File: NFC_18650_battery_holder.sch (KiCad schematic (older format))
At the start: 2 parts

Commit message: Schematic done.
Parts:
- added J?: Conn_01x06_Female, symbol Connector:Conn_01x06_Female
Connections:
- net at AE?.1: now also U?.3 (AC1)
- net at AE?.2: now also U?.2 (AC0)
- net Sheet5FAF080E/BATT_RET: now reaches U?.4 (VSS)
- net Sheet5FAF080E/BATT_RET: now also J?.6 (Pin_6)
- net at U?.5 (SDA): now also J?.5 (Pin_5)
- net at U?.6 (SCL): now also J?.4 (Pin_4)
- net at U?.7 (GPO_(OD)): now also J?.3 (Pin_3)
- net at U?.8 (VCC): now also J?.2 (Pin_2)
- new net +BATT: J?.1 (Pin_1)
- no-connect marks 0 -> 1
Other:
- moved on the sheet: AE?, U?
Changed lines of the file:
@@
 $Descr A4 11693 8268
 encoding utf-8
-Sheet 1 1
+Sheet 1 2
 Title ""
 Date ""
@@
 L Device:Antenna_Loop AE?
 U 1 1 5FAE3919
-P 6700 2400
-F 0 "AE?" H 6930 2414 50  0000 L CNN
-F 1 "Antenna_Loop" H 6930 2323 50  0000 L CNN
-F 2 "" H 6700 2400 50  0001 C CNN
-F 3 "~" H 6700 2400 50  0001 C CNN
-	1    6700 2400
+P 7050 2400
+F 0 "AE?" H 7280 2414 50  0000 L CNN
+F 1 "Antenna_Loop" H 7280 2323 50  0000 L CNN
+F 2 "" H 7050 2400 50  0001 C CNN
+F 3 "~" H 7050 2400 50  0001 C CNN
+	1    7050 2400
 	1    0    0    -1
 $EndComp
@@
 L NFC_18659_battery_holder:ST25DV_8p U?
 U 1 1 5FAE5573
-P 8600 2550
-F 0 "U?" H 8600 2565 50  0000 C CNN
-F 1 "ST25DV_8p" H 8600 2474 50  0000 C CNN
-F 2 "" H 8600 2550 50  0001 C CNN
-F 3 "" H 8600 2550 50  0001 C CNN
-	1    8600 2550
+P 8150 2800
+F 0 "U?" H 8150 2815 50  0000 C CNN
+F 1 "ST25DV_8p" H 8150 2724 50  0000 C CNN
+F 2 "" H 8150 2800 50  0001 C CNN
+F 3 "" H 8150 2800 50  0001 C CNN
+	1    8150 2800
 	1    0    0    -1
 $EndComp
+$Sheet
+S 5550 3000 1050 500
+U 5FAF080F
+F0 "Sheet5FAF080E" 50
+F1 "battery_3s_18650.sch" 50
+F2 "BATT_OUT" I R 6600 3100 50
+F3 "BATT_RET" I R 6600 3350 50
+$EndSheet
+Wire Wire Line
+	7650 3150 7150 3150
+Wire Wire Line
+	7150 3150 7150 2600
+Wire Wire Line
+	7050 2600 7050 3250
+Wire Wire Line
+	7050 3250 7650 3250
+Wire Wire Line
+	7650 3350 7350 3350
+$Comp
+L power:+BATT #PWR?
+U 1 1 5FAF9693
+P 6800 2900
+F 0 "#PWR?" H 6800 2750 50  0001 C CNN
+F 1 "+BATT" H 6815 3073 50  0000 C CNN
+F 2 "" H 6800 2900 50  0001 C CNN
+F 3 "" H 6800 2900 50  0001 C CNN
+	1    6800 2900
+	1    0    0    -1
+$EndComp
+Wire Wire Line
+	6800 3100 6800 2900
+Wire Wire Line
+	6600 3100 6800 3100
+Wire Wire Line
+	9400 3350 8650 3350
+Wire Wire Line
+	8650 3250 9400 3250
+Wire Wire Line
+	9400 3150 8650 3150
+Wire Wire Line
+	8650 3050 9400 3050
+Wire Wire Line
+	9400 2950 9100 2950
+Wire Wire Line
+	9100 2950 9100 2800
+$Comp
+L power:+BATT #PWR?
+U 1 1 5FAFB912
+P 9100 2800
+F 0 "#PWR?" H 9100 2650 50  0001 C CNN
+F 1 "+BATT" H 9115 2973 50  0000 C CNN
+F 2 "" H 9100 2800 50  0001 C CNN
+F 3 "" H 9100 2800 50  0001 C CNN
+	1    9100 2800
+	1    0    0    -1
+$EndComp
+$Comp
+L Connector:Conn_01x06_Female J?
+U 1 1 5FAFC15A
+P 9600 3150
+F 0 "J?" H 9628 3126 50  0000 L CNN
+F 1 "Conn_01x06_Female" H 9628 3035 50  0000 L CNN
+F 2 "" H 9600 3150 50  0001 C CNN
+F 3 "~" H 9600 3150 50  0001 C CNN
+	1    9600 3150
+	1    0    0    -1
+$EndComp
+Wire Wire Line
+	9400 3450 9250 3450
+Wire Wire Line
+	9250 3450 9250 3650
+Wire Wire Line
+	9250 3650 7350 3650
+Wire Wire Line
+	7350 3650 7350 3350
+Connection ~ 7350 3350
+Wire Wire Line
+	7350 3350 6600 3350
+NoConn ~ 7650 3050
 $EndSCHEMATC

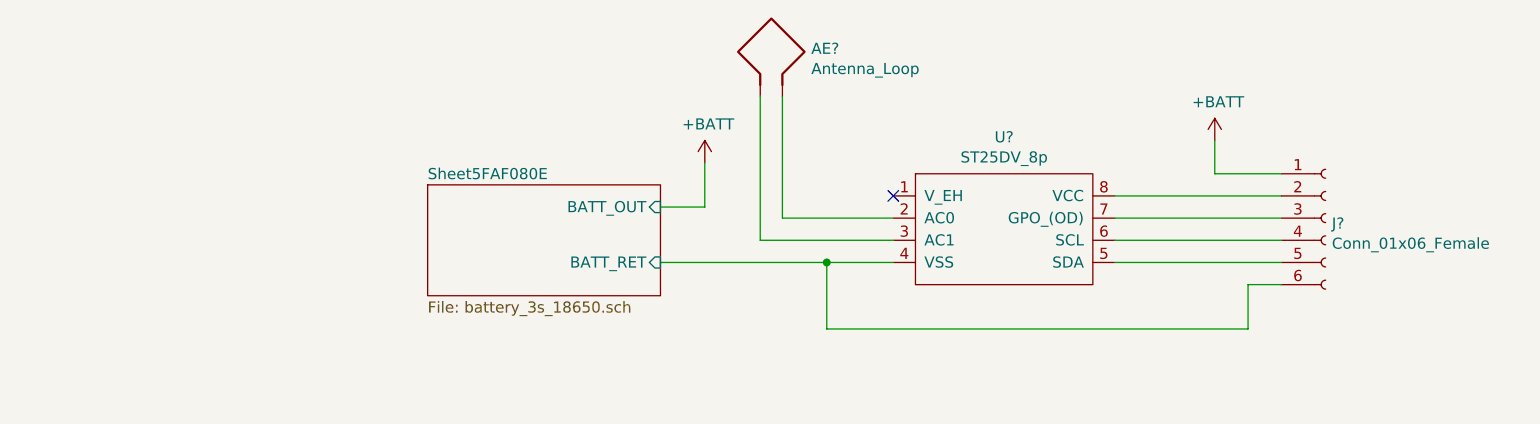
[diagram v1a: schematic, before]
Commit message: Library files added from NFC_hatch projekt. Started to work at the layout. 18650 holder footprint became wider 18 to 22mm.
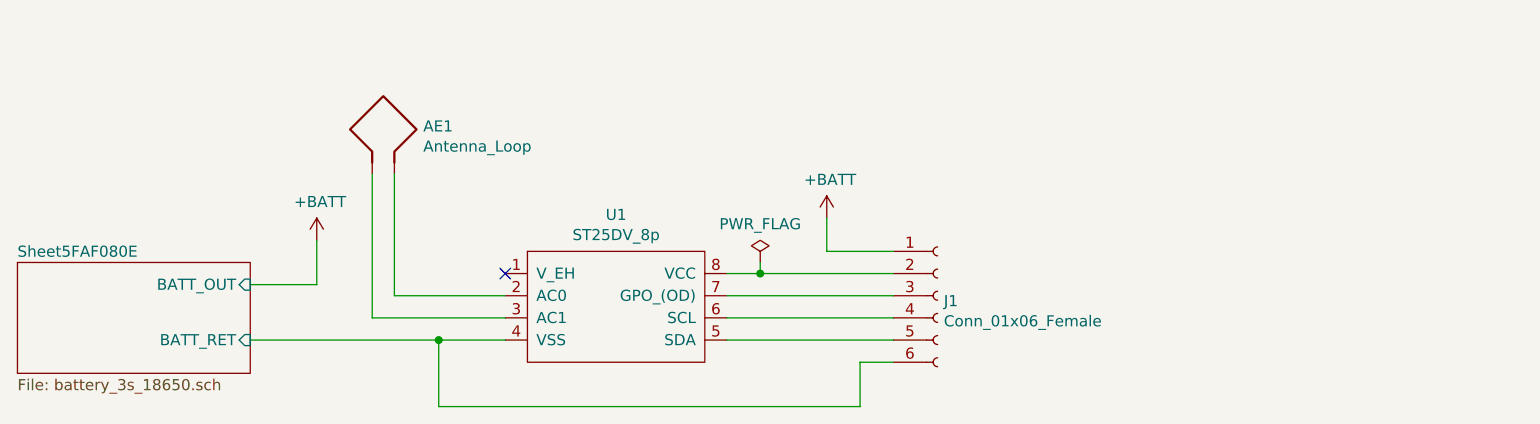
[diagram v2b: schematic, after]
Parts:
- J1: renamed from J?; footprint (none) -> Connector_JST:JST_XH_B6B-XH-A_1x06_P2.50mm_Vertical
- U1: renamed from U?; footprint (none) -> Package_SO:TSSOP-8_4.4x3mm_P0.65mm
- gave numbers to parts that had none: 1
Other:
- moved on the sheet: AE1, J1, U1
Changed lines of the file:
@@
 $EndDescr
 $Comp
-L Device:Antenna_Loop AE?
+L Device:Antenna_Loop AE1
 U 1 1 5FAE3919
-P 7050 2400
-F 0 "AE?" H 7280 2414 50  0000 L CNN
-F 1 "Antenna_Loop" H 7280 2323 50  0000 L CNN
-F 2 "" H 7050 2400 50  0001 C CNN
-F 3 "~" H 7050 2400 50  0001 C CNN
-	1    7050 2400
+P 5300 2750
+F 0 "AE1" H 5530 2764 50  0000 L CNN
+F 1 "Antenna_Loop" H 5530 2673 50  0000 L CNN
+F 2 "" H 5300 2750 50  0001 C CNN
+F 3 "~" H 5300 2750 50  0001 C CNN
+	1    5300 2750
 	1    0    0    -1
 $EndComp
 $Comp
-L NFC_18659_battery_holder:ST25DV_8p U?
+L NFC_18659_battery_holder:ST25DV_8p U1
 U 1 1 5FAE5573
-P 8150 2800
-F 0 "U?" H 8150 2815 50  0000 C CNN
-F 1 "ST25DV_8p" H 8150 2724 50  0000 C CNN
-F 2 "" H 8150 2800 50  0001 C CNN
-F 3 "" H 8150 2800 50  0001 C CNN
-	1    8150 2800
+P 6400 3150
+F 0 "U1" H 6400 3165 50  0000 C CNN
+F 1 "ST25DV_8p" H 6400 3074 50  0000 C CNN
+F 2 "Package_SO:TSSOP-8_4.4x3mm_P0.65mm" H 6400 3150 50  0001 C CNN
+F 3 "" H 6400 3150 50  0001 C CNN
+	1    6400 3150
 	1    0    0    -1
 $EndComp
 $Sheet
-S 5550 3000 1050 500
+S 3700 3350 1050 500
 U 5FAF080F
 F0 "Sheet5FAF080E" 50
 F1 "battery_3s_18650.sch" 50
-F2 "BATT_OUT" I R 6600 3100 50
-F3 "BATT_RET" I R 6600 3350 50
+F2 "BATT_OUT" I R 4750 3450 50
+F3 "BATT_RET" I R 4750 3700 50
 $EndSheet
 Wire Wire Line
-	7650 3150 7150 3150
+	5900 3500 5400 3500
 Wire Wire Line
-	7150 3150 7150 2600
+	5400 3500 5400 2950
 Wire Wire Line
-	7050 2600 7050 3250
+	5300 2950 5300 3600
 Wire Wire Line
-	7050 3250 7650 3250
+	5300 3600 5900 3600
 Wire Wire Line
-	7650 3350 7350 3350
+	5900 3700 5600 3700
 $Comp
-L power:+BATT #PWR?
+L power:+BATT #PWR0101
 U 1 1 5FAF9693
-P 6800 2900
-F 0 "#PWR?" H 6800 2750 50  0001 C CNN
-F 1 "+BATT" H 6815 3073 50  0000 C CNN
-F 2 "" H 6800 2900 50  0001 C CNN
-F 3 "" H 6800 2900 50  0001 C CNN
-	1    6800 2900
+P 5050 3250
+F 0 "#PWR0101" H 5050 3100 50  0001 C CNN
+F 1 "+BATT" H 5065 3423 50  0000 C CNN
+F 2 "" H 5050 3250 50  0001 C CNN
+F 3 "" H 5050 3250 50  0001 C CNN
+	1    5050 3250
 	1    0    0    -1
 $EndComp
 Wire Wire Line
-	6800 3100 6800 2900
+	5050 3450 5050 3250
 Wire Wire Line
-	6600 3100 6800 3100
+	4750 3450 5050 3450
 Wire Wire Line
-	9400 3350 8650 3350
+	7650 3700 6900 3700
 Wire Wire Line
-	8650 3250 9400 3250
+	6900 3600 7650 3600
 Wire Wire Line
-	9400 3150 8650 3150
+	7650 3500 6900 3500
 Wire Wire Line
-	8650 3050 9400 3050
+	6900 3400 7050 3400
 Wire Wire Line
-	9400 2950 9100 2950
+	7650 3300 7350 3300
 Wire Wire Line
-	9100 2950 9100 2800
+	7350 3300 7350 3150
 $Comp
-L power:+BATT #PWR?
+L power:+BATT #PWR0102
 U 1 1 5FAFB912
-P 9100 2800
-F 0 "#PWR?" H 9100 2650 50  0001 C CNN
-F 1 "+BATT" H 9115 2973 50  0000 C CNN
-F 2 "" H 9100 2800 50  0001 C CNN
-F 3 "" H 9100 2800 50  0001 C CNN
-	1    9100 2800
+P 7350 3150
+F 0 "#PWR0102" H 7350 3000 50  0001 C CNN
+F 1 "+BATT" H 7365 3323 50  0000 C CNN
+F 2 "" H 7350 3150 50  0001 C CNN
+F 3 "" H 7350 3150 50  0001 C CNN
+	1    7350 3150
 	1    0    0    -1
 $EndComp
 $Comp
-L Connector:Conn_01x06_Female J?
+L Connector:Conn_01x06_Female J1
 U 1 1 5FAFC15A
-P 9600 3150
-F 0 "J?" H 9628 3126 50  0000 L CNN
-F 1 "Conn_01x06_Female" H 9628 3035 50  0000 L CNN
-F 2 "" H 9600 3150 50  0001 C CNN
-F 3 "~" H 9600 3150 50  0001 C CNN
-	1    9600 3150
+P 7850 3500
+F 0 "J1" H 7878 3476 50  0000 L CNN
+F 1 "Conn_01x06_Female" H 7878 3385 50  0000 L CNN
+F 2 "Connector_JST:JST_XH_B6B-XH-A_1x06_P2.50mm_Vertical" H 7850 3500 50  0001 C CNN
+F 3 "~" H 7850 3500 50  0001 C CNN
+	1    7850 3500
 	1    0    0    -1
 $EndComp
 Wire Wire Line
-	9400 3450 9250 3450
+	7650 3800 7500 3800
 Wire Wire Line
-	9250 3450 9250 3650
+	7500 3800 7500 4000
 Wire Wire Line
-	9250 3650 7350 3650
+	5600 4000 5600 3700
+Connection ~ 5600 3700
 Wire Wire Line
-	7350 3650 7350 3350
-Connection ~ 7350 3350
+	5600 3700 4750 3700
+NoConn ~ 5900 3400
+$Comp
+L power:PWR_FLAG #FLG0102
+U 1 1 5FB0134E
+P 7050 3350
+F 0 "#FLG0102" H 7050 3425 50  0001 C CNN
+F 1 "PWR_FLAG" H 7050 3523 50  0000 C CNN
+F 2 "" H 7050 3350 50  0001 C CNN
+F 3 "~" H 7050 3350 50  0001 C CNN
+	1    7050 3350
+	1    0    0    -1
+$EndComp
 Wire Wire Line
-	7350 3350 6600 3350
-NoConn ~ 7650 3050
+	7050 3350 7050 3400
+Connection ~ 7050 3400
+Wire Wire Line
+	7050 3400 7650 3400
+Wire Wire Line
+	7500 4000 5600 4000
 $EndSCHEMATC

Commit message: 4.1uH antenna project done. Antenna was added to project via bitmap.
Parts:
- AE1: footprint (none) -> NFC_18650_battery_holder:Antenna_4.1uH
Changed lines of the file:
@@
 F 0 "AE1" H 5530 2764 50  0000 L CNN
 F 1 "Antenna_Loop" H 5530 2673 50  0000 L CNN
-F 2 "" H 5300 2750 50  0001 C CNN
+F 2 "NFC_18650_battery_holder:Antenna_4.1uH" H 5300 2750 50  0001 C CNN
 F 3 "~" H 5300 2750 50  0001 C CNN
 	1    5300 2750

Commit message: Antenna footprints done.
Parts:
- AE1: footprint NFC_18650_battery_holder:Antenna_4.1uH -> NFC_18650_battery_holder:Antenna_4.58uH
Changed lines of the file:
@@
 F 0 "AE1" H 5530 2764 50  0000 L CNN
 F 1 "Antenna_Loop" H 5530 2673 50  0000 L CNN
-F 2 "NFC_18650_battery_holder:Antenna_4.1uH" H 5300 2750 50  0001 C CNN
+F 2 "NFC_18650_battery_holder:Antenna_4.58uH" H 5300 2750 50  0001 C CNN
 F 3 "~" H 5300 2750 50  0001 C CNN
 	1    5300 2750

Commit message: 4.32uH Antenna board done!
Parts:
- AE1: footprint NFC_18650_battery_holder:Antenna_4.58uH -> NFC_18650_battery_holder:Antenna_4.32uH
- U1: footprint Package_SO:TSSOP-8_4.4x3mm_P0.65mm -> Package_SO:SOP-8_3.9x4.9mm_P1.27mm
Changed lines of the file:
@@
 F 0 "AE1" H 5530 2764 50  0000 L CNN
 F 1 "Antenna_Loop" H 5530 2673 50  0000 L CNN
-F 2 "NFC_18650_battery_holder:Antenna_4.58uH" H 5300 2750 50  0001 C CNN
+F 2 "NFC_18650_battery_holder:Antenna_4.32uH" H 5300 2750 50  0001 C CNN
 F 3 "~" H 5300 2750 50  0001 C CNN
 	1    5300 2750
@@
 F 0 "U1" H 6400 3165 50  0000 C CNN
 F 1 "ST25DV_8p" H 6400 3074 50  0000 C CNN
-F 2 "Package_SO:TSSOP-8_4.4x3mm_P0.65mm" H 6400 3150 50  0001 C CNN
+F 2 "Package_SO:SOP-8_3.9x4.9mm_P1.27mm" H 6400 3150 50  0001 C CNN
 F 3 "" H 6400 3150 50  0001 C CNN
 	1    6400 3150

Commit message: 4.10uH Antenna created. Couryard was added to battery footprint and vias were removed around battery as a result.
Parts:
- AE1: footprint NFC_18650_battery_holder:Antenna_4.32uH -> NFC_18650_battery_holder:Antenna_4.10uH
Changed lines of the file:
@@
 F 0 "AE1" H 5530 2764 50  0000 L CNN
 F 1 "Antenna_Loop" H 5530 2673 50  0000 L CNN
-F 2 "NFC_18650_battery_holder:Antenna_4.32uH" H 5300 2750 50  0001 C CNN
+F 2 "NFC_18650_battery_holder:Antenna_4.10uH" H 5300 2750 50  0001 C CNN
 F 3 "~" H 5300 2750 50  0001 C CNN
 	1    5300 2750
